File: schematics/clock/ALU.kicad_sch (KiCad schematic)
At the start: 0 parts

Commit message: add alu
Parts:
- added D19, D20, D21, D22, D23, D24, D25, D26: LED, symbol Device:LED
- added RLED26, RLED27, RLED28, RLED29, RLED30, RLED31, RLED32, RLED33: 469, symbol Device:R
- added U14, U15: 74LS283, symbol 74xx:74LS283
- added U16, U17: 74LS86, symbol 74xx:74LS86
- added U18: 74LS245, symbol 74xx:74LS245
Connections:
- net A1: now also U14.5 (A1)
- net A2: now also U14.3 (A2)
- net A3: now also U14.14 (A3)
- net A4: now also U14.12 (A4)
- net A5: now also U15.5 (A1)
- net A6: now also U15.3 (A2)
- net A7: now also U15.14 (A3)
- net A8: now also U15.12 (A4)
- net B1: now also U17.13
- net B2: now also U17.10
- net B3: now also U17.5
- net B4: now also U17.2
- net B5: now also U16.2
- net B6: now also U16.5
- net B7: now also U16.10
- net B8: now also U16.13
- new net: U14.6 (B1), U17.11
- new net: U14.15 (B3), U17.6
- new net: U15.15 (B3), U16.8
- new net: D26.1 (K), RLED33.1
- new net: D26.2 (A), U15.10 (S4), U18.9 (A7)
- new net: D23.1 (K), RLED30.1
- new net: D23.2 (A), U15.4 (S1), U18.6 (A4)
- new net: D22.1 (K), RLED29.1
- new net: D22.2 (A), U14.10 (S4), U18.5 (A3)
- new net: D19.2 (A), U14.4 (S1), U18.2 (A0)
- new net: D20.2 (A), U14.1 (S2), U18.3 (A1)
- new net: D21.2 (A), U14.13 (S3), U18.4 (A2)
- new net: D24.2 (A), U15.1 (S2), U18.7 (A5)
- new net: D25.2 (A), U15.13 (S3), U18.8 (A6)
- new net: U14.2 (B2), U17.8
- new net: U15.6 (B1), U16.3
- new net: D25.1 (K), RLED32.1
- new net: D21.1 (K), RLED28.1
- new net: D24.1 (K), RLED31.1
- new net: D19.1 (K), RLED26.1
- new net: U14.11 (B4), U17.3
- new net: U14.9 (C4), U15.7 (C0)
- new net: U15.11 (B4), U16.11
- new net: U15.2 (B2), U16.6
- new net: D20.1 (K), RLED27.1
- new net +5V: U14.16 (VCC), U15.16 (VCC), U18.1 (A->B), U18.10 (GND)
- new net BUS1: U18.18 (B0)
- new net BUS2: U18.17 (B1)
- new net BUS3: U18.16 (B2)
- new net BUS4: U18.15 (B3)
- new net BUS5: U18.14 (B4)
- new net BUS6: U18.13 (B5)
- new net BUS7: U18.12 (B6)
- new net BUS8: U18.11 (B7)
- new net GND: RLED26.2, RLED27.2, RLED28.2, RLED29.2, RLED30.2, RLED31.2, RLED32.2, RLED33.2, U14.8 (GND), U15.8 (GND), U18.20 (VCC)
- new net enable: U18.19 (CE)
- new net ~{SU}: U14.7 (C0), U16.1, U16.12, U16.4, U16.9, U17.1, U17.12, U17.4, U17.9

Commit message: fix usb 2
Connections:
- net at D26.2 (A), U15.10 (S4): now also U18.2 (A0); no longer U18.9 (A7)
- net at D23.2 (A), U15.4 (S1): now also U18.5 (A3); no longer U18.6 (A4)
- net at D22.2 (A), U14.10 (S4): now also U18.6 (A4); no longer U18.5 (A3)
- net at D19.2 (A), U14.4 (S1): now also U18.9 (A7); no longer U18.2 (A0)
- net at D20.2 (A), U14.1 (S2): now also U18.8 (A6); no longer U18.3 (A1)
- net at D21.2 (A), U14.13 (S3): now also U18.7 (A5); no longer U18.4 (A2)
- net at D24.2 (A), U15.1 (S2): now also U18.4 (A2); no longer U18.7 (A5)
- net at D25.2 (A), U15.13 (S3): now also U18.3 (A1); no longer U18.8 (A6)

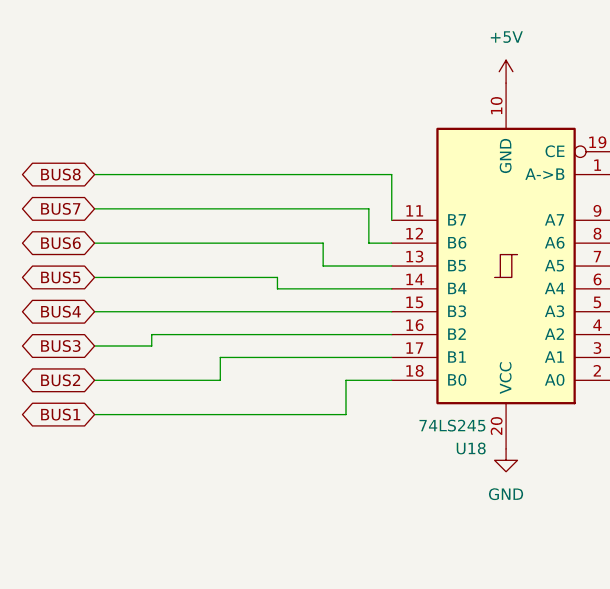
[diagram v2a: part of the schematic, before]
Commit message: add ram, change bus
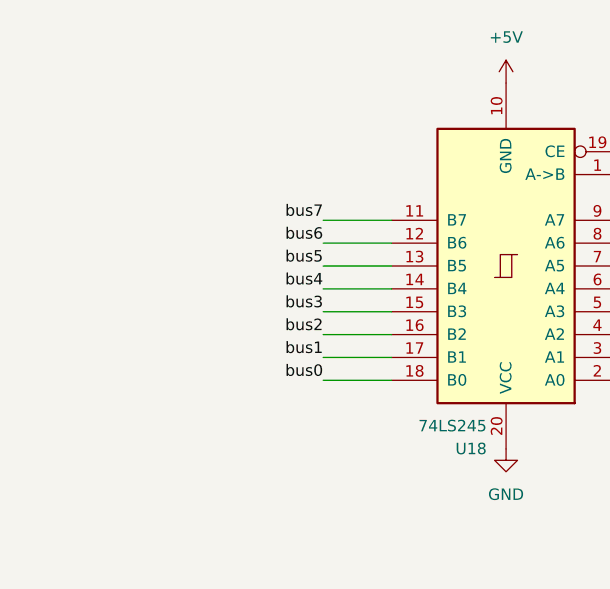
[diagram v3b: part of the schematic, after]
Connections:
- net BUS1 renamed bus0
- net BUS2 renamed bus1
- net BUS3 renamed bus2
- net BUS4 renamed bus3
- net BUS5 renamed bus4
- net BUS6 renamed bus5
- net BUS7 renamed bus6
- net BUS8 renamed bus7
